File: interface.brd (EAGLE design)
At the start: 28.3 x 18.3 mm, 14 parts, among them IC2 ATTINY87/167AUTOMOTIVE, U1 ISL3179EIBZ

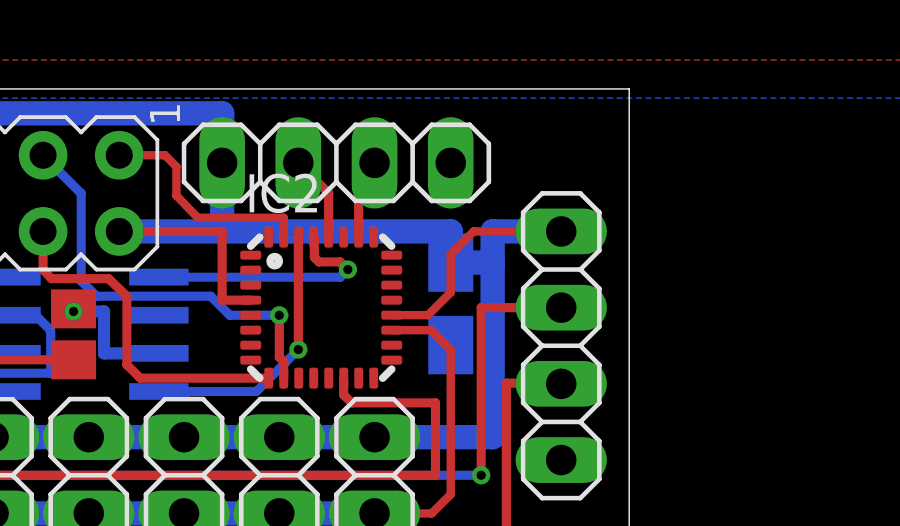
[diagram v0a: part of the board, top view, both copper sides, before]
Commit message: forgot i2c pullups
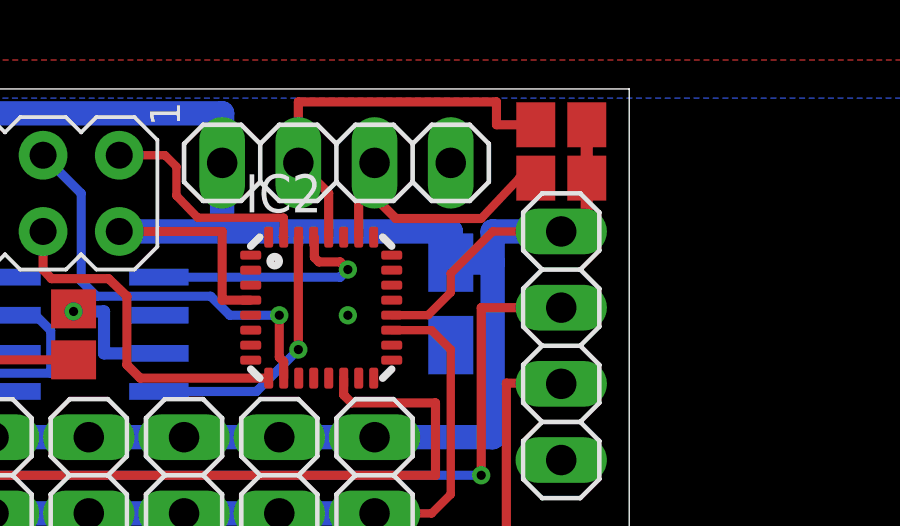
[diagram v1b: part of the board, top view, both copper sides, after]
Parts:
- added R3, R4: 10k, resistor:R0805
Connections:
- net SCL: now also R3.1
- net SDA: now also R4.1
- net VCC: now also R3.2, R4.2
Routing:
- net SDA: track 2.90 -> 13.6 mm
- net SCL: track 2.69 -> 10.1 mm
- net VCC: track 87.9 -> 91.9 mm
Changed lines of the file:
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@@
 <attribute name="VALUE" x="4.572" y="10.287" size="1.27" layer="27" rot="R270"/>
+</element>
+<element name="R3" library="resistor" package="R0805" value="10k" x="26.67" y="17.653" smashed="yes">
+<attribute name="VALUE" x="25.908" y="15.367" size="1.27" layer="27"/>
+</element>
+<element name="R4" library="resistor" package="R0805" value="10k" x="26.67" y="19.431" smashed="yes">
+<attribute name="VALUE" x="25.908" y="17.145" size="1.27" layer="27"/>
 </element>
 </elements>
@@
 <vertex x="-5.08" y="-2.54"/>
 </polygon>
+<via x="19.558" y="13.081" extent="1-16" drill="0.3048" diameter="0.3048"/>
+<wire x1="16.319" y1="13.085" x2="13.2588" y2="13.081" width="0" layer="19" extent="1-16"/>
 </signal>
 <signal name="VCC">
@@
 <wire x1="21.019" y1="13.085" x2="22.229" y2="13.085" width="0.2794" layer="1"/>
 <wire x1="22.229" y1="13.085" x2="22.987" y2="13.843" width="0.2794" layer="1"/>
-<wire x1="22.987" y1="13.843" x2="22.987" y2="15.113" width="0.2794" layer="1"/>
-<wire x1="22.987" y1="15.113" x2="23.749" y2="15.875" width="0.2794" layer="1"/>
-<wire x1="23.749" y1="15.875" x2="26.67" y2="15.875" width="0.2794" layer="1"/>
+<wire x1="22.987" y1="13.843" x2="22.987" y2="14.478" width="0.2794" layer="1"/>
+<wire x1="22.987" y1="14.478" x2="24.384" y2="15.875" width="0.2794" layer="1"/>
+<wire x1="24.384" y1="15.875" x2="26.67" y2="15.875" width="0.2794" layer="1"/>
 <wire x1="7.747" y1="9.017" x2="7.747" y2="10.453" width="0.3048" layer="1"/>
 <wire x1="7.747" y1="10.453" x2="6.731" y2="11.469" width="0.3048" layer="1"/>
@@
 <wire x1="8.3312" y1="14.351" x2="3.937" y2="14.351" width="0.3048" layer="16"/>
 <wire x1="3.937" y1="14.351" x2="2.413" y2="15.875" width="0.3048" layer="16"/>
+<contactref element="R4" pad="2"/>
+<contactref element="R3" pad="2"/>
+<wire x1="27.52" y1="17.653" x2="27.52" y2="19.431" width="0.4064" layer="1"/>
+<wire x1="26.67" y1="15.875" x2="27.52" y2="15.875" width="0.4064" layer="1"/>
+<wire x1="27.52" y1="15.875" x2="27.52" y2="17.653" width="0.4064" layer="1"/>
 </signal>
 <signal name="AY">
@@
 <wire x1="17.907" y1="18.161" x2="18.919" y2="17.149" width="0.3048" layer="1"/>
 <wire x1="18.919" y1="17.149" x2="18.919" y2="15.685" width="0.3048" layer="1"/>
+<contactref element="R4" pad="1"/>
+<wire x1="25.82" y1="19.431" x2="24.511" y2="19.431" width="0.3048" layer="1"/>
+<wire x1="24.511" y1="19.431" x2="24.511" y2="20.193" width="0.3048" layer="1"/>
+<wire x1="24.511" y1="20.193" x2="17.907" y2="20.193" width="0.3048" layer="1"/>
+<wire x1="17.907" y1="20.193" x2="17.907" y2="18.161" width="0.3048" layer="1"/>
 </signal>
 <signal name="SCL">
@@
 <wire x1="20.447" y1="18.161" x2="19.919" y2="17.633" width="0.3048" layer="1"/>
 <wire x1="19.919" y1="17.633" x2="19.919" y2="15.685" width="0.3048" layer="1"/>
+<contactref element="R3" pad="1"/>
+<wire x1="25.82" y1="17.653" x2="25.273" y2="17.653" width="0.3048" layer="1"/>
+<wire x1="25.273" y1="17.653" x2="24.003" y2="16.3068" width="0.2794" layer="1"/>
+<wire x1="24.003" y1="16.3068" x2="21.1582" y2="16.3068" width="0.3048" layer="1"/>
+<wire x1="21.1582" y1="16.3068" x2="20.447" y2="17.018" width="0.3048" layer="1"/>
+<wire x1="20.447" y1="17.018" x2="20.447" y2="18.161" width="0.3048" layer="1"/>
 </signal>
 <signal name="1W">

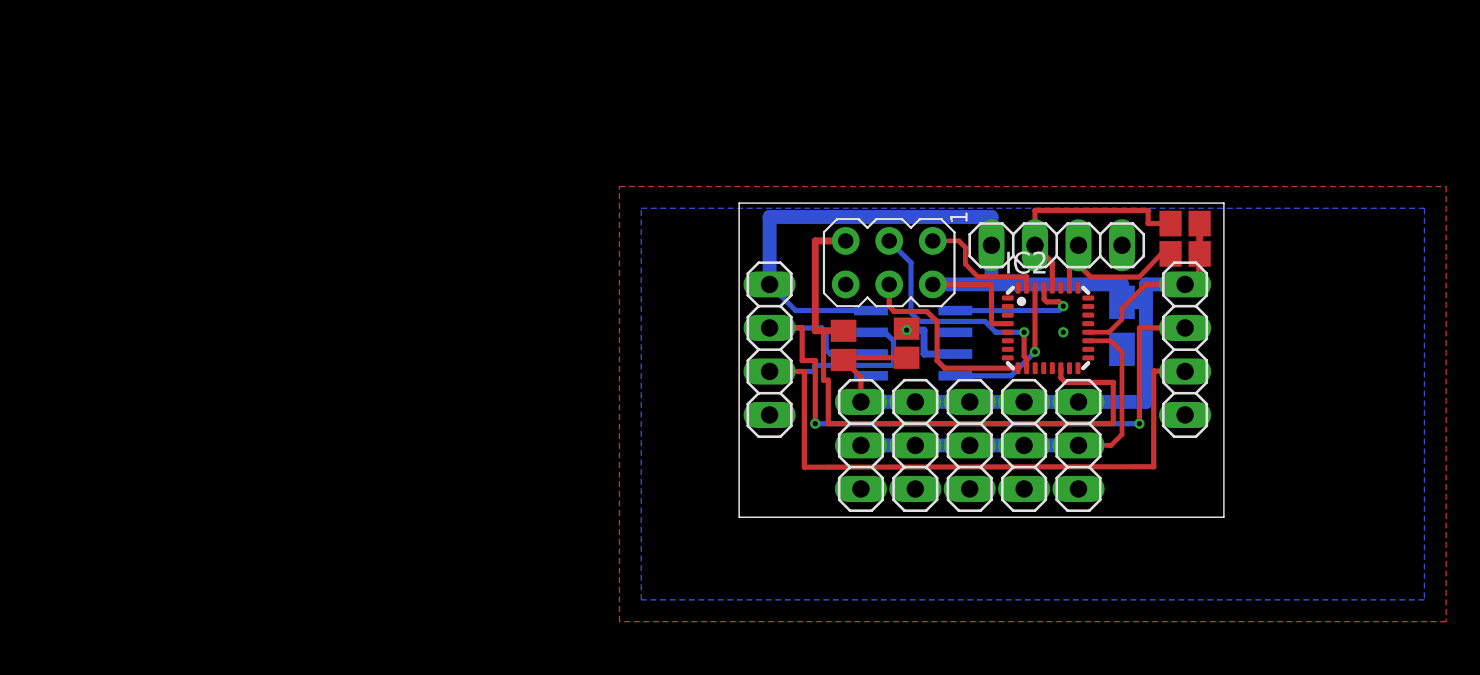
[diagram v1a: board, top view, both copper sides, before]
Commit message: now uses an avr supported by arduino
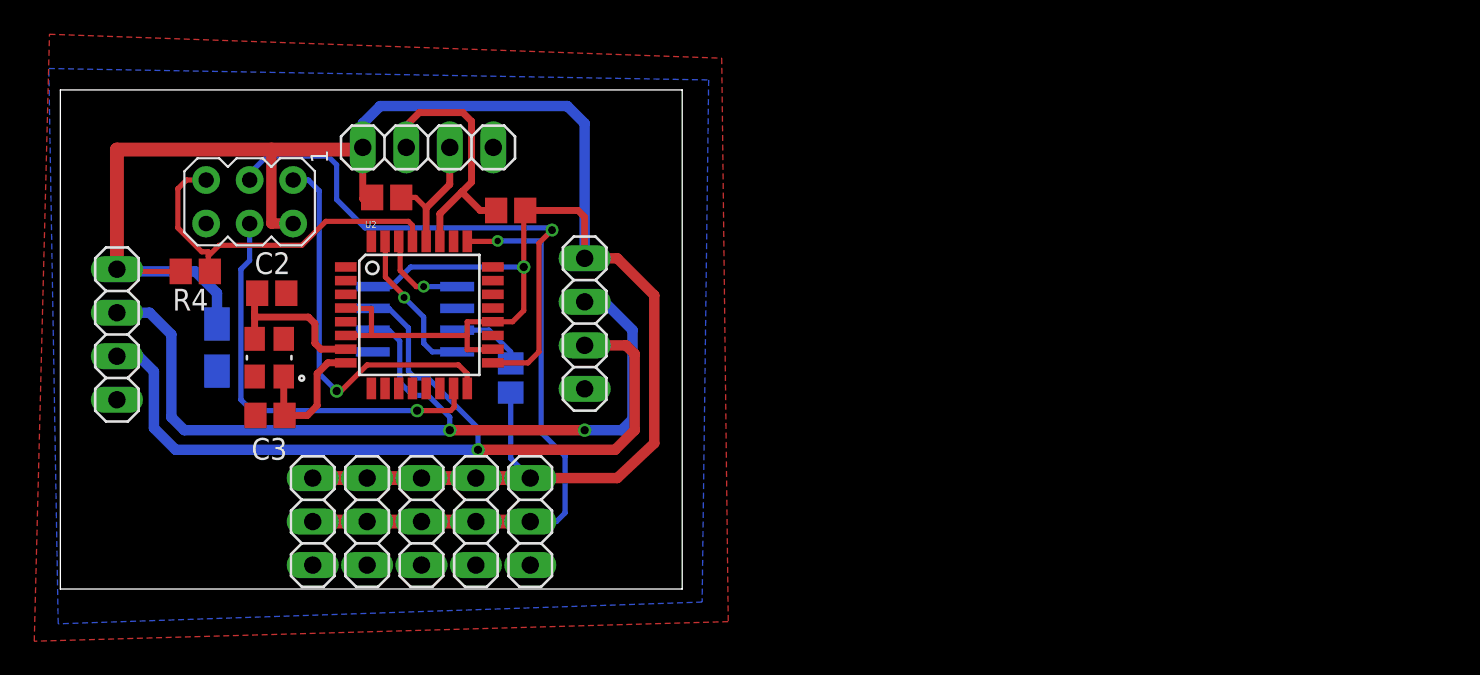
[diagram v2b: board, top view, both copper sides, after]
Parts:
- removed C5: 22uF, resistor:A/3216-18R
- removed IC2: ATTINY87/167AUTOMOTIVE, attiny87_167_automotive:MLF32
- added C1: 22uF, resistor:A/3216-18R
- added C2, C3: 22pF, resistor:C0805
- added U2: ATMEGA328P, SparkFun-DigitalIC:TQFP32-08
- added XTAL1: 7M-16.000MAAJ-T, TXC-7M-16.000MAAJ-T:TXC_7M-16.000MAAJ-T
- R2: value 10K -> 10k
- R4: value 10k -> 10K
- moved JP1 62.4 mm to (-35.7, 13.0)
- moved R4 57.9 mm to (-31.1, 16.6), turned to 180 degrees
- moved R3 46.7 mm to (-19.9, 21.0), turned to 180 degrees
- moved ISP1 37.5 mm to (-27.9, 20.7)
- moved JP3 37.1 mm to (-17.5, 23.9)
- moved JP7 32.3 mm to (-21.1, 2.03)
- moved JP8 32.3 mm to (-24.3, 2.03)
- moved JP4 32.3 mm to (-11.6, 2.03)
- moved JP5 32.3 mm to (-14.7, 2.03)
- moved JP6 32.3 mm to (-17.9, 2.03)
- moved U1 29.1 mm to (-18.3, 13.8)
- moved R1 23.2 mm to (-12.7, 10.4), flipped to the bottom
- moved R2 21.0 mm to (-12.7, 20.2), turned to 0 degrees
- moved JP2 10.9 mm to (-8.38, 13.6)
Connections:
- new net N$2: C2.2, U2.7, XTAL1.3
- new net N$3: C3.2, U2.8, XTAL1.1
- net !RESET: now also R4.1, U2.29; no longer IC2.14, R2.1
- net 1W: now also U2.25; no longer IC2.19
- net GND: now also C1.-, C2.1, C3.1, U2.21, U2.3, U2.5; no longer C5.-, IC2.21, IC2.5
- net MISO: now also U2.16; no longer IC2.31
- net MOSI: now also U2.15; no longer IC2.9
- net RX: now also U2.30; no longer IC2.29
- net SCK: now also U2.17; no longer IC2.10
- net SCL: now also U2.28; no longer IC2.26
- net SDA: now also R2.1, U2.27; no longer IC2.28, R4.1
- net TX: now also U2.31; no longer IC2.30
- net VCC: now also C1.+, U2.18, U2.20, U2.4, U2.6; no longer C5.+, IC2.20, IC2.4
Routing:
- net VCC: track 91.9 -> 143.6 mm, vias 0 -> 1
- net SCK: track 14.0 -> 31.9 mm
- net !RESET: track 37.2 -> 21.5 mm
- net MISO: track 7.59 -> 23.2 mm, vias 0 -> 1
- net MOSI: track 11.6 -> 24.4 mm, vias 0 -> 1
- net 1W: track 23.0 -> 35.7 mm, vias 0 -> 1
- net AY: track 42.6 -> 53.5 mm
- net N$2: track 0.00 -> 9.58 mm
- net BZ: track 46.0 -> 54.3 mm, vias 0 -> 1
- net N$3: track 0.00 -> 8.27 mm
- net RX: track 8.37 -> 5.45 mm
- net SCL: track 10.1 -> 7.77 mm
- net SDA: track 13.6 -> 15.8 mm
- net N$1: track 4.33 -> 4.32 mm, vias 1 -> 0
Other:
- board size 28.3 x 18.3 mm -> 36.3 x 29.1 mm

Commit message: added optional 3v3 reg
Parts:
- added C4: 10uF, resistor:A/3216-18R
- added C5: 22uF, resistor:A/3216-18R
- added JP9: JUMPER-31-2, SparkFun-Passives:SJ_3_PASTE1&2
- added U$1: TLV1117-33CDCY, basestation:SOT223
- JP3: value (none) -> I2C
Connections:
- new net 3V3: C5.+, JP9.3, U$1.2, U$1.4
- new net VIN: C1.+, C4.+, JP1.1, JP2.1, JP4.1, JP5.1, JP6.1, JP7.1, JP8.1, JP9.1, U$1.3
- net GND: now also C4.-, C5.-, U$1.1
- net VCC: now also JP9.2; no longer C1.+, JP1.1, JP2.1, JP4.1, JP5.1, JP6.1, JP7.1, JP8.1
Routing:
- net VIN: track 0.00 -> 92.7 mm, vias 0 -> 1
- net VCC: track 143.6 -> 90.5 mm, vias 1 -> 2
- net 3V3: track 0.00 -> 30.6 mm

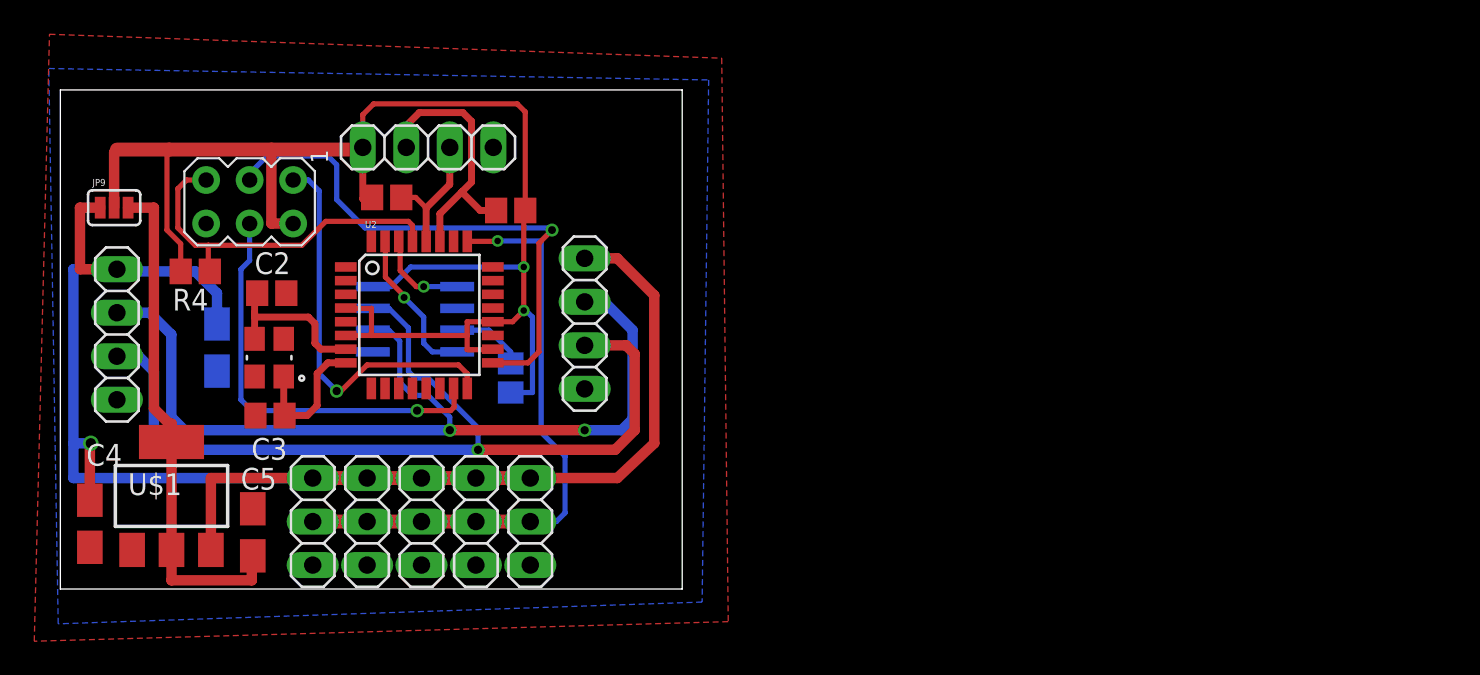
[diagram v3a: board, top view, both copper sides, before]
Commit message: now has 2 I2C busses
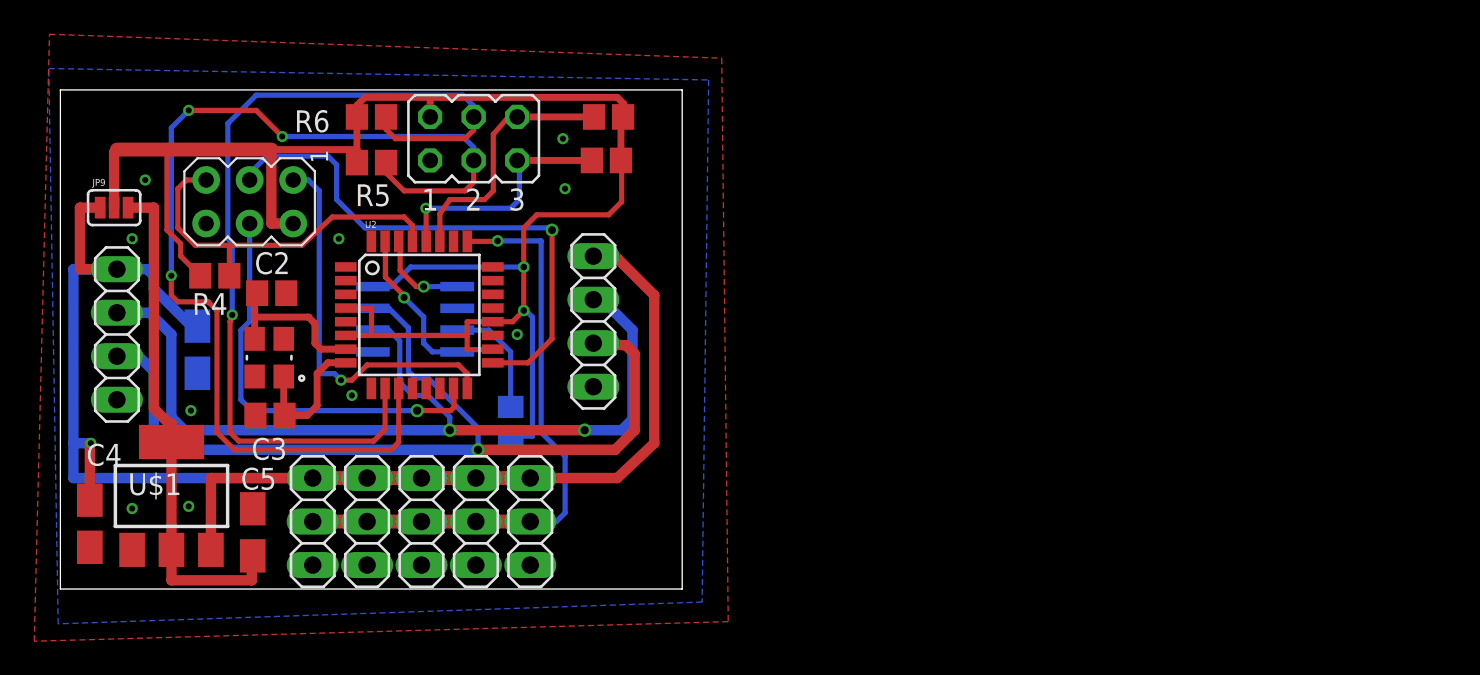
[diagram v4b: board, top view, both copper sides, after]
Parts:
- added R5, R6: 10k, resistor:R0805
- JP3: device pinhead:1X04 -> jumper:JP3Q
- moved R3 13.0 mm to (-7.11, 23.1), turned to 0 degrees
- moved R2 7.90 mm to (-6.99, 25.7)
- moved JP3 2.71 mm to (-14.9, 24.4)
- moved R1 2.54 mm to (-12.7, 7.87)
- moved R4 1.17 mm to (-30.0, 16.4)
- moved C1 1.15 mm to (-31.0, 12.1)
- moved JP2 0.52 mm to (-7.87, 13.7)
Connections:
- removed net SCL: JP3.3, R3.1, U2.28
- removed net SDA: JP3.2, R2.1, U2.27
- new net SCL1: JP3.5, R3.1, U2.28
- new net SCL2: JP3.3, R5.1, U2.11
- new net SDA1: JP3.6, R2.1, U2.27
- new net SDA2: JP3.4, R6.1, U2.10
- net GND: now also JP3.1; no longer JP3.4
- net VCC: now also JP3.2, R5.2, R6.2; no longer JP3.1
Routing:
- net SCL2: track 0.00 -> 61.6 mm, vias 0 -> 3
- net SDA2: track 0.00 -> 53.1 mm, vias 0 -> 1
- net SDA: track 15.8 -> 0.00 mm
- net SDA1: track 0.00 -> 15.0 mm
- net SCL1: track 0.00 -> 14.3 mm, vias 0 -> 1
- net VCC: track 90.5 -> 103.9 mm
- net SCL: track 7.77 -> 0.00 mm
- net N$1: track 4.32 -> 6.86 mm
- net VIN: track 92.7 -> 90.5 mm
- net MISO: track 23.2 -> 22.7 mm
- net BZ: track 54.3 -> 53.8 mm
